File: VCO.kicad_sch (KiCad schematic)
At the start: 36 parts

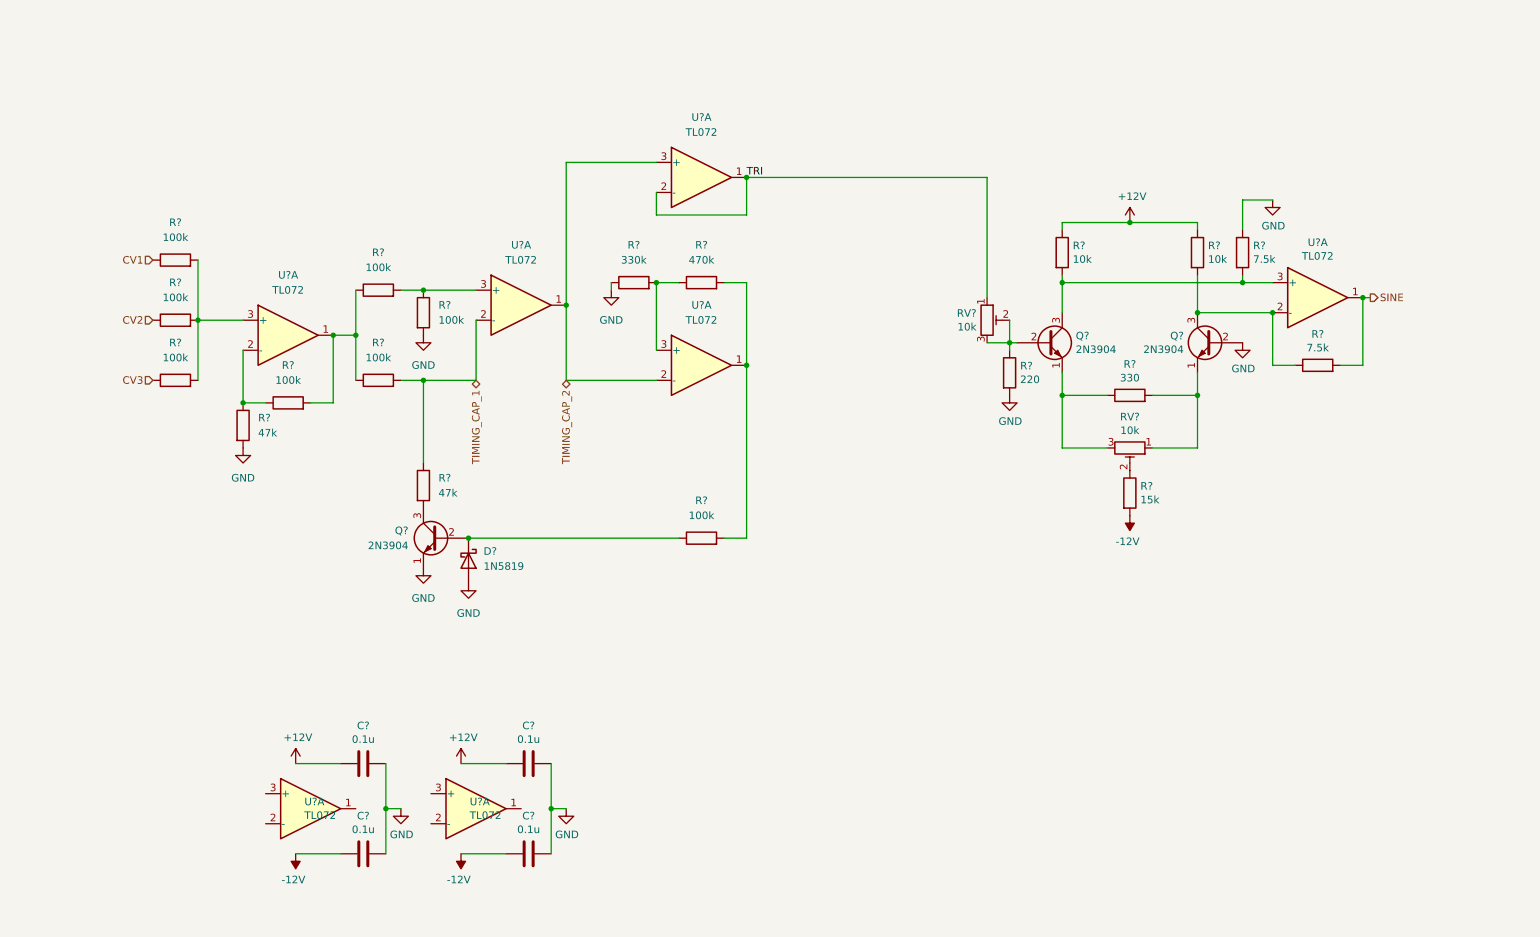
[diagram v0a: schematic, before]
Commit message: Finish schematic
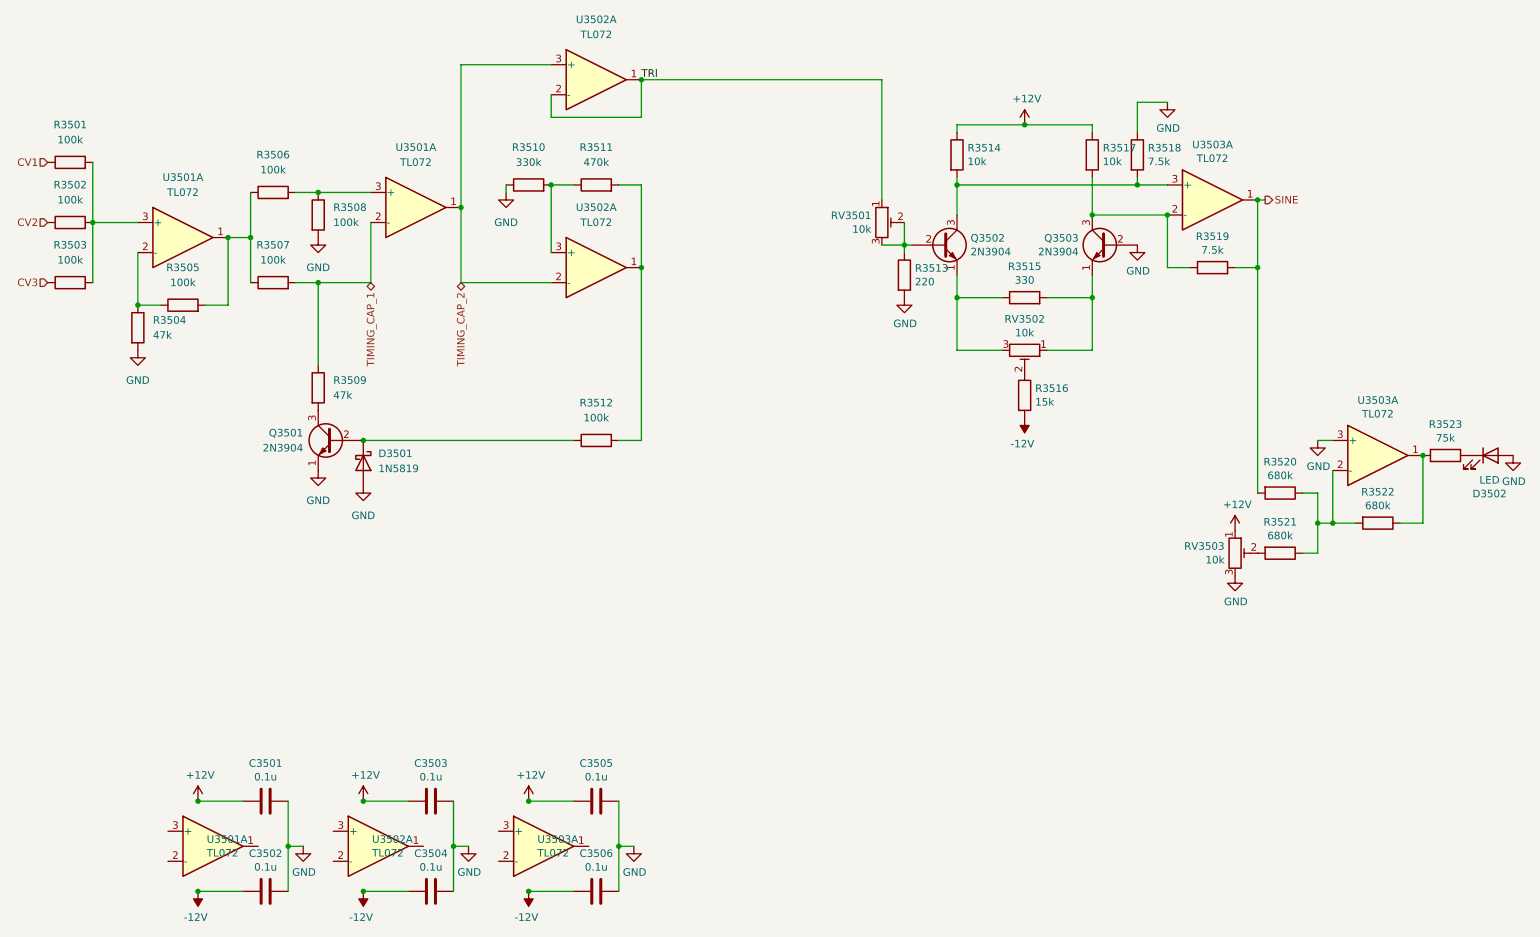
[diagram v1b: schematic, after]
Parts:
- added C3505, C3506: 0.1u, Capacitor_THT:C_Disc_D5.0mm_W2.5mm_P5.00mm, symbol Device:C
- added D3502: LED, LED_THT:LED_D5.0mm, symbol Device:LED
- added R3520, R3521, R3522: 680k, Resistor_THT:R_Axial_DIN0207_L6.3mm_D2.5mm_P7.62mm_Horizontal, symbol Device:R
- added R3523: 75k, Resistor_THT:R_Axial_DIN0207_L6.3mm_D2.5mm_P7.62mm_Horizontal, symbol Device:R
- added RV3503: 10k, Custom:Potentiometer_Runtron_RM-065_Vertical_Improved, symbol Device:R_Potentiometer_Trim
- added U3503 (x2): TL072, Package_DIP:DIP-8_W7.62mm_Socket, symbol Amplifier_Operational:TL072
- Q3501, Q3502, Q3503: renamed from Q?; footprint Package_TO_SOT_THT:TO-92_Inline -> Package_TO_SOT_THT:TO-92_HandSolder
- R3501, R3502, R3503, R3504, R3505, R3506, R3507, R3508, R3509, R3510, R3511, R3512: renamed from R?; footprint (none) -> Resistor_THT:R_Axial_DIN0207_L6.3mm_D2.5mm_P7.62mm_Horizontal
- U3501, U3502: renamed from U?; footprint (none) -> Package_DIP:DIP-8_W7.62mm_Socket
- gave numbers to parts that had none: 17
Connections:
- net +12V: now also C3505.1, RV3503.1
- net -12V: now also C3506.1
- net GND: now also C3505.2, C3506.2, D3502.2 (A), RV3503.3, U3503.3 (+)
- net SINE: now also R3520.2
- new net: D3502.1 (K), R3523.1
- new net: R3522.1, R3523.2, U3503.1
- new net: R3520.1, R3521.1, R3522.2, U3503.2 (-)
- new net: R3521.2, RV3503.2
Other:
- moved on the sheet: C3501, C3502, C3503, C3504, D3501, Q3501, Q3502, Q3503, R3501, R3502, R3503, R3504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

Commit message: Update VCO
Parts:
- added C3503: 10n, symbol Device:C
- renumbered C3503 to C3504, C3504 to C3505, C3505 to C3506, C3506 to C3507
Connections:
- net TIMING_CAP_1: no longer names the net of R3507.2, R3509.1, U3501.2 (-)
- net TIMING_CAP_1: now also C3503.1
- net TIMING_CAP_2: no longer names the net of U3501.1, U3502.2 (-), U3502.3 (+)
- net TIMING_CAP_2: now also C3503.2
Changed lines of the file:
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@@
     (rev "1.0")
   )
-  (junction (at 81.28 165.1) (diameter 0) (color 0 0 0 0)
-  )
   (junction (at 35.56 67.31) (diameter 0) (color 0 0 0 0)
   )
@@
   (junction (at 217.17 66.04) (diameter 0) (color 0 0 0 0)
   )
-  (junction (at 109.22 180.34) (diameter 0) (color 0 0 0 0)
-  )
   (junction (at 113.03 60.96) (diameter 0) (color 0 0 0 0)
   )
@@
   (junction (at 81.28 104.14) (diameter 0) (color 0 0 0 0)
   )
+  (junction (at 97.79 77.47) (diameter 0) (color 0 0 0 0)
+  )
   (junction (at 212.09 60.96) (diameter 0) (color 0 0 0 0)
   )
@@
   (junction (at 204.47 80.01) (diameter 0) (color 0 0 0 0)
   )
+  (junction (at 82.55 77.47) (diameter 0) (color 0 0 0 0)
+  )
   (junction (at 245.11 118.11) (diameter 0) (color 0 0 0 0)
   )
@@
   (junction (at 68.58 172.72) (diameter 0) (color 0 0 0 0)
   )
-  (junction (at 109.22 165.1) (diameter 0) (color 0 0 0 0)
-  )
   (junction (at 97.79 64.77) (diameter 0) (color 0 0 0 0)
   )
@@
   (junction (at 124.46 172.72) (diameter 0) (color 0 0 0 0)
   )
-  (junction (at 81.28 180.34) (diameter 0) (color 0 0 0 0)
-  )
   (junction (at 172.72 71.12) (diameter 0) (color 0 0 0 0)
   )
@@
   (junction (at 128.27 74.93) (diameter 0) (color 0 0 0 0)
   )
-  (junction (at 53.34 180.34) (diameter 0) (color 0 0 0 0)
-  )
   (junction (at 181.61 80.01) (diameter 0) (color 0 0 0 0)
   )
@@
   (junction (at 58.42 69.85) (diameter 0) (color 0 0 0 0)
   )
-  (junction (at 53.34 165.1) (diameter 0) (color 0 0 0 0)
-  )
   (junction (at 232.41 63.5) (diameter 0) (color 0 0 0 0)
   )
@@
     (stroke (width 0) (type default) (color 0 0 0 0))
   )
+  (wire (pts (xy 82.55 77.47) (xy 86.36 77.47))
+    (stroke (width 0) (type default) (color 0 0 0 0))
+  )
   (wire (pts (xy 128.27 49.53) (xy 128.27 43.18))
     (stroke (width 0) (type default) (color 0 0 0 0))
@@
   )
   (wire (pts (xy 204.47 66.04) (xy 217.17 66.04))
+    (stroke (width 0) (type default) (color 0 0 0 0))
+  )
+  (wire (pts (xy 93.98 77.47) (xy 97.79 77.47))
     (stroke (width 0) (type default) (color 0 0 0 0))
   )
@@
     (effects (font (size 1.27 1.27)) (justify left))
   )
-  (hierarchical_label "TIMING_CAP_2" (shape bidirectional) (at 97.79 77.47 270)
-    (effects (font (size 1.27 1.27)) (justify right))
-  )
   (hierarchical_label "CV3" (shape input) (at 27.94 77.47 180)
     (effects (font (size 1.27 1.27)) (justify right))
@@
   )
   (hierarchical_label "CV1" (shape input) (at 27.94 57.15 180)
-    (effects (font (size 1.27 1.27)) (justify right))
-  )
-  (hierarchical_label "TIMING_CAP_1" (shape bidirectional) (at 82.55 77.47 270)
     (effects (font (size 1.27 1.27)) (justify right))
   )
@@
   (symbol (lib_id "Device:C") (at 120.65 180.34 90)
     (in_bom yes) (on_board yes)
-    (property "Reference" "C3506" (id 0) (at 120.65 173.9392 90))
+    (property "Reference" "C3507" (id 0) (at 120.65 173.9392 90))
     (property "Value" "0.1u" (id 1) (at 120.65 176.2506 90))
     (property "Footprint" "Capacitor_THT:C_Disc_D5.0mm_W2.5mm_P5.00mm" (id 2) (at 124.46 179.3748 0)
@@
     (pin "2")
   )
+  (symbol (lib_id "Device:C") (at 90.17 77.47 90)
+    (in_bom yes) (on_board yes) (fields_autoplaced)
+    (property "Reference" "C3503" (id 0) (at 90.17 69.85 90))
+    (property "Value" "10n" (id 1) (at 90.17 72.39 90))
+    (property "Footprint" "" (id 2) (at 93.98 76.5048 0)
+      (effects (font (size 1.27 1.27)) hide)
+    )
+    (property "Datasheet" "~" (id 3) (at 90.17 77.47 0)
+      (effects (font (size 1.27 1.27)) hide)
+    )
+    (pin "1")
+    (pin "2")
+  )
   (symbol (lib_id "power:GND") (at 127 172.72 0)
     (in_bom yes) (on_board yes)
@@
   (symbol (lib_id "Device:C") (at 120.65 165.1 90)
     (in_bom yes) (on_board yes)
-    (property "Reference" "C3505" (id 0) (at 120.65 158.6992 90))
+    (property "Reference" "C3506" (id 0) (at 120.65 158.6992 90))
     (property "Value" "0.1u" (id 1) (at 120.65 161.0106 90))
     (property "Footprint" "Capacitor_THT:C_Disc_D5.0mm_W2.5mm_P5.00mm" (id 2) (at 124.46 164.1348 0)
@@
   (symbol (lib_id "Device:C") (at 92.71 165.1 90)
     (in_bom yes) (on_board yes)
-    (property "Reference" "C3503" (id 0) (at 92.71 158.6992 90))
+    (property "Reference" "C3504" (id 0) (at 92.71 158.6992 90))
     (property "Value" "0.1u" (id 1) (at 92.71 161.0106 90))
     (property "Footprint" "Capacitor_THT:C_Disc_D5.0mm_W2.5mm_P5.00mm" (id 2) (at 96.52 164.1348 0)
@@
   (symbol (lib_id "Device:C") (at 92.71 180.34 90)
     (in_bom yes) (on_board yes)
-    (property "Reference" "C3504" (id 0) (at 92.71 173.9392 90))
+    (property "Reference" "C3505" (id 0) (at 92.71 173.9392 90))
     (property "Value" "0.1u" (id 1) (at 92.71 176.2506 90))
     (property "Footprint" "Capacitor_THT:C_Disc_D5.0mm_W2.5mm_P5.00mm" (id 2) (at 96.52 179.3748 0)

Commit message: Finish PCB
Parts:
- C3503: footprint (none) -> Capacitor_THT:C_Disc_D5.0mm_W2.5mm_P5.00mm
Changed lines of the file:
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@@
     (property "Reference" "C3503" (id 0) (at 90.17 69.85 90))
     (property "Value" "10n" (id 1) (at 90.17 72.39 90))
-    (property "Footprint" "" (id 2) (at 93.98 76.5048 0)
+    (property "Footprint" "Capacitor_THT:C_Disc_D5.0mm_W2.5mm_P5.00mm" (id 2) (at 93.98 76.5048 0)
       (effects (font (size 1.27 1.27)) hide)
     )
